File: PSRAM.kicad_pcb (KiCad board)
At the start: 2 copper layers, 19.1 x 16.3 mm, 4 parts, among them J1 Conn_02x06_Top_Bottom, U1 LY68L6400

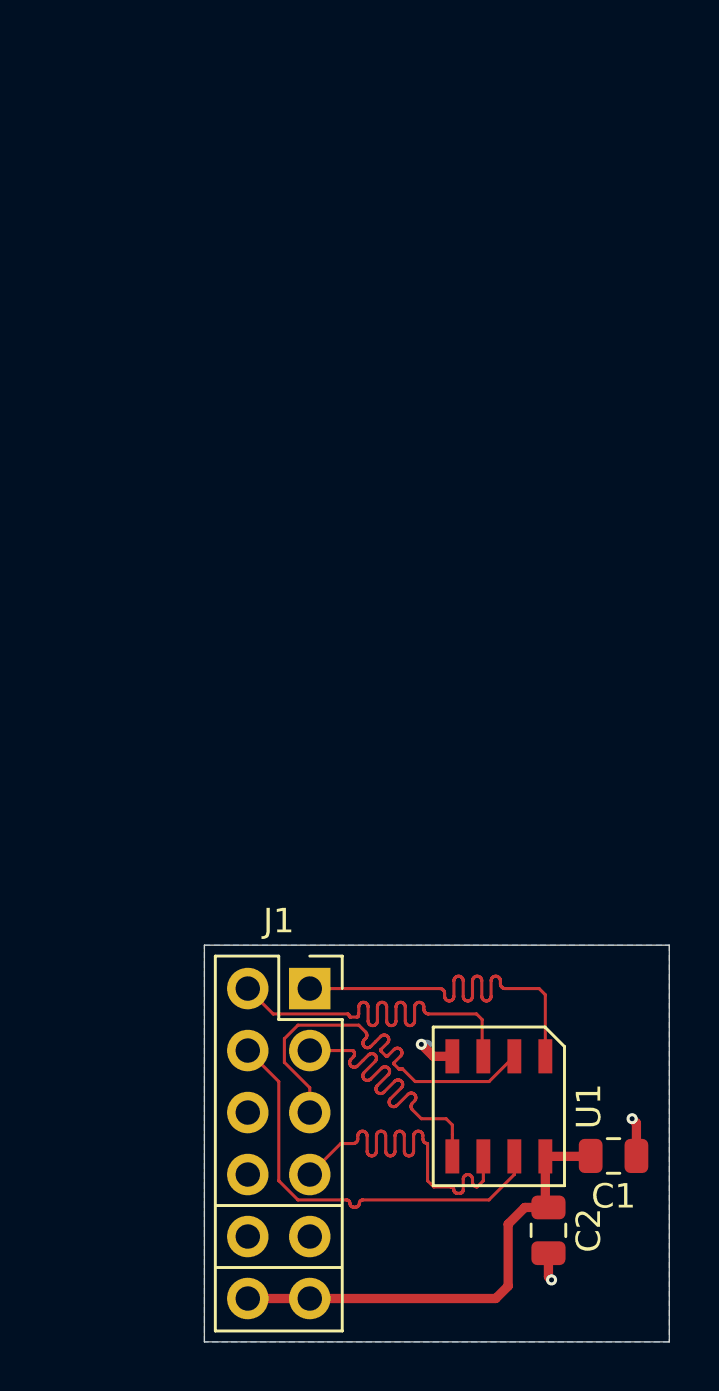
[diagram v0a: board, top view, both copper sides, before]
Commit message: New revision with 4 layers
This is version 0.2 and has been tested successfully up to 139 MHz.

Signed-off-by: Oguz Meteer <info@guztech.nl>
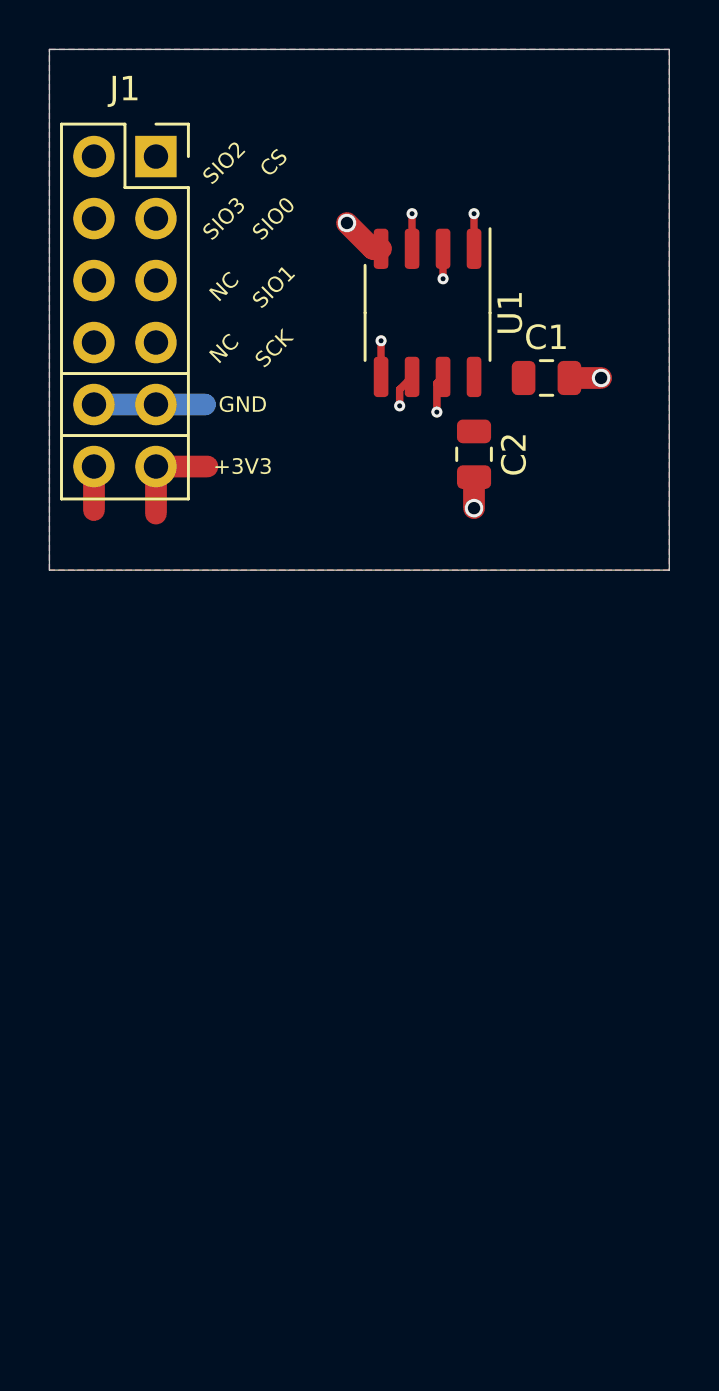
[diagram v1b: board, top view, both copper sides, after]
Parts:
- U1: footprint GuzTech_Footprints:SOP-8_150mil -> Package_SO:SOP-8_3.9x4.9mm_P1.27mm
- moved J1 34.7 mm to (132.9, 67.5)
- moved U1 32.6 mm to (144.0, 73.9)
- moved C1 32.0 mm to (148.9, 76.6)
- moved C2 31.9 mm to (145.9, 79.7)
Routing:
- net +3V3: track 19.4 -> 5.82 mm
- net SDI-SIO[0]: track 15.0 -> 21.2 mm, vias 0 -> 1
- net CS: track 17.2 -> 21.7 mm, vias 0 -> 1
- net GND: track 4.47 -> 8.96 mm
- net SDO-SIO[1]: track 17.2 -> 21.6 mm, vias 0 -> 1
- net SIO[2]: track 17.3 -> 21.6 mm, vias 0 -> 1
- net SCK: track 17.3 -> 21.6 mm, vias 0 -> 1
- net SIO[3]: track 17.3 -> 21.7 mm, vias 0 -> 1
- added copper zone on F.Cu, net +3V3
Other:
- board size 19.1 x 16.3 mm -> 25.4 x 21.3 mm
- copper layers 2 -> 4
- net class 5mil added: clearance 0.127, trace_width 0.127, via_dia 0.4572, via_drill 0.2032
- net class Default: clearance 0.254 -> 0.2032; trace_width 0.381 -> 0.3048
- net class data removed
- net class power added: clearance 0.254, trace_width 0.889, via_dia 0.762, via_drill 0.508
- net class signals added: clearance 0.254, trace_width 0.508, via_dia 0.5588, via_drill 0.381
- rule trace_clearance: 0.254 -> 0.2032
- board text added: "PSRAM PMOD v0.2 GuzTech"
- board text removed: "PSRAM PMOD v0.1 GuzTech"
